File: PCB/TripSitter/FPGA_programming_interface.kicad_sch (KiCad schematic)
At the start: 10 parts, among them IC1 MT25QL256ABA1EW9-0SIT, J1 Conn_ARM_JTAG_SWD_20, U1 XC7A100T-FGG484

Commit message: before
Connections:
- net +3V3 is gone; now on net +3.3V: J1.2 (VCC/NC), R38.1, U1.U11 (M0_0)
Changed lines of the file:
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@@
   (junction (at 147.32 44.45) (diameter 0) (color 0 0 0 0)
   )
+  (junction (at 181.61 92.71) (diameter 0) (color 0 0 0 0)
+  )
   (junction (at 101.6 57.15) (diameter 0) (color 0 0 0 0)
   )
@@
   )
   (junction (at 184.15 142.24) (diameter 0) (color 0 0 0 0)
-  )
-  (junction (at 181.61 92.71) (diameter 0) (color 0 0 0 0)
   )
   (junction (at 43.18 95.25) (diameter 0) (color 0 0 0 0)
@@
     )
   )
-  (symbol (lib_id "fpga-rescue:+3.3V-power") (at 181.61 92.71 0) (unit 1)
-    (in_bom yes) (on_board yes) (dnp no)
-    (property "Reference" "#PWR047" (at 181.61 96.52 0)
-      (effects (font (size 1.27 1.27)) hide)
-    )
-    (property "Value" "+3.3V" (at 181.61 89.154 0)
-      (effects (font (size 1.27 1.27)))
-    )
-    (property "Footprint" "" (at 181.61 92.71 0)
-      (effects (font (size 1.27 1.27)) hide)
-    )
-    (property "Datasheet" "" (at 181.61 92.71 0)
-      (effects (font (size 1.27 1.27)) hide)
-    )
-    (pin "1")
-    (instances
-      (project "TripSitter"
-        (path "/5ab65702-9689-4dfd-8f10-6407062323a6/095fe883-dc50-4e06-a886-995eeb7c2300/a589e109-056b-42fc-a935-6e0e623ed03d"
-          (reference "#PWR047") (unit 1)
-        )
-      )
-      (project "fpga"
-        (path "/6f02ba16-07ff-46df-8179-c80a375dc867"
-          (reference "#PWR0302") (unit 1)
-        )
-      )
-    )
-  )
   (symbol (lib_id "Device:C_Small") (at 86.36 44.45 0) (unit 1)
     (in_bom yes) (on_board yes) (dnp no) (fields_autoplaced)
@@
         )
       )
+    )
+  )
+  (symbol (lib_id "power:+3.3V") (at 181.61 92.71 0) (mirror y) (unit 1)
+    (in_bom yes) (on_board yes) (dnp no)
+    (property "Reference" "#PWR011" (at 181.61 96.52 0)
+      (effects (font (size 1.27 1.27)) hide)
+    )
+    (property "Value" "+3.3V" (at 181.61 87.63 0)
+      (effects (font (size 1.27 1.27)))
+    )
+    (property "Footprint" "" (at 181.61 92.71 0)
+      (effects (font (size 1.27 1.27)) hide)
+    )
+    (property "Datasheet" "" (at 181.61 92.71 0)
+      (effects (font (size 1.27 1.27)) hide)
+    )
+    (pin "1")
+    (instances
+      (project "TripSitter"
+        (path "/5ab65702-9689-4dfd-8f10-6407062323a6/095fe883-dc50-4e06-a886-995eeb7c2300"
+          (reference "#PWR011") (unit 1)
+        )
+        (path "/5ab65702-9689-4dfd-8f10-6407062323a6/095fe883-dc50-4e06-a886-995eeb7c2300/ae3612c6-9651-4a37-8de7-7277774520fa"
+          (reference "#PWR014") (unit 1)
+        )
+        (path "/5ab65702-9689-4dfd-8f10-6407062323a6/095fe883-dc50-4e06-a886-995eeb7c2300/a589e109-056b-42fc-a935-6e0e623ed03d"
+          (reference "#PWR065") (unit 1)
+        )
+      )

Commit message: more pcb routing
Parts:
- added R20, R21: 10k, Resistor_SMD:R_0805_2012Metric_Pad1.20x1.40mm_HandSolder, symbol Device:R
- added R23, R24: 4.7k, Resistor_SMD:R_0603_1608Metric_Pad0.98x0.95mm_HandSolder, symbol Device:R
- C39: footprint Capacitor_SMD:C_1210_3225Metric_Pad1.33x2.70mm_HandSolder -> Capacitor_SMD:C_0603_1608Metric_Pad1.08x0.95mm_HandSolder; Component name CL21A476MQYNNNG -> CL10A476MR8NZNE; DK_Detail_Page https://www.digikey.no/product-detail/no/murata-electronics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 -> https://www.digikey.no/no/products/detail/samsung-electro-m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
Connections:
- net +3.3V: now also R20.1, R21.2
- net FPGA_PROGRAM_B: now also R24.1
- net at J1.7 (TMS/SWDIO), U1.T13 (TMS_0): now also R20.2
- net at U1.U12 (INIT_B_0): now also R23.1
- net at J1.9 (TCK/SWDCLK), U1.V12 (TCK_0): now also R21.1
- new net +3V3: R23.2, R24.2
- no-connect marks 15 -> 14

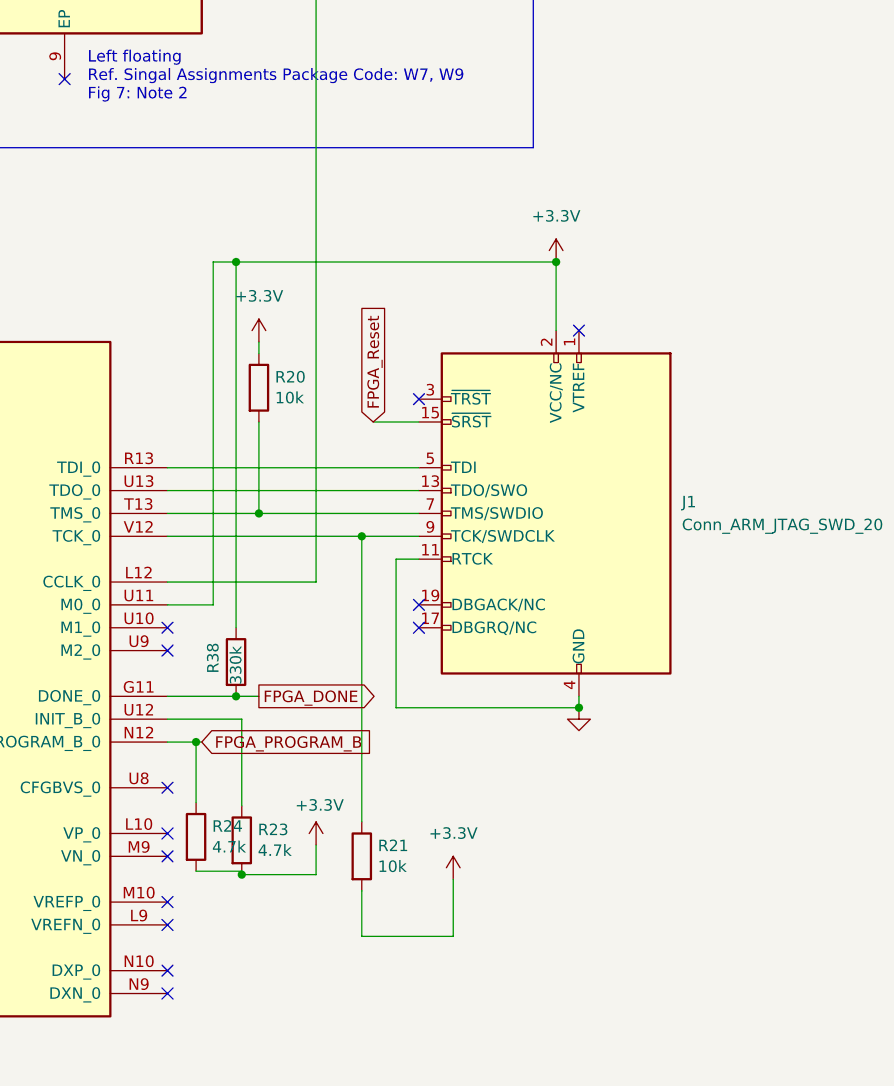
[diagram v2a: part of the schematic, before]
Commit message: pcb: Finalized routing without DDR3
Added ground and power plane, layed out all the components, fanned out
BGA. QSPI between FPGA->MCU->SRAM and MCU->SRAM is routed. Most is done
but DRC does not pass so do not produce.
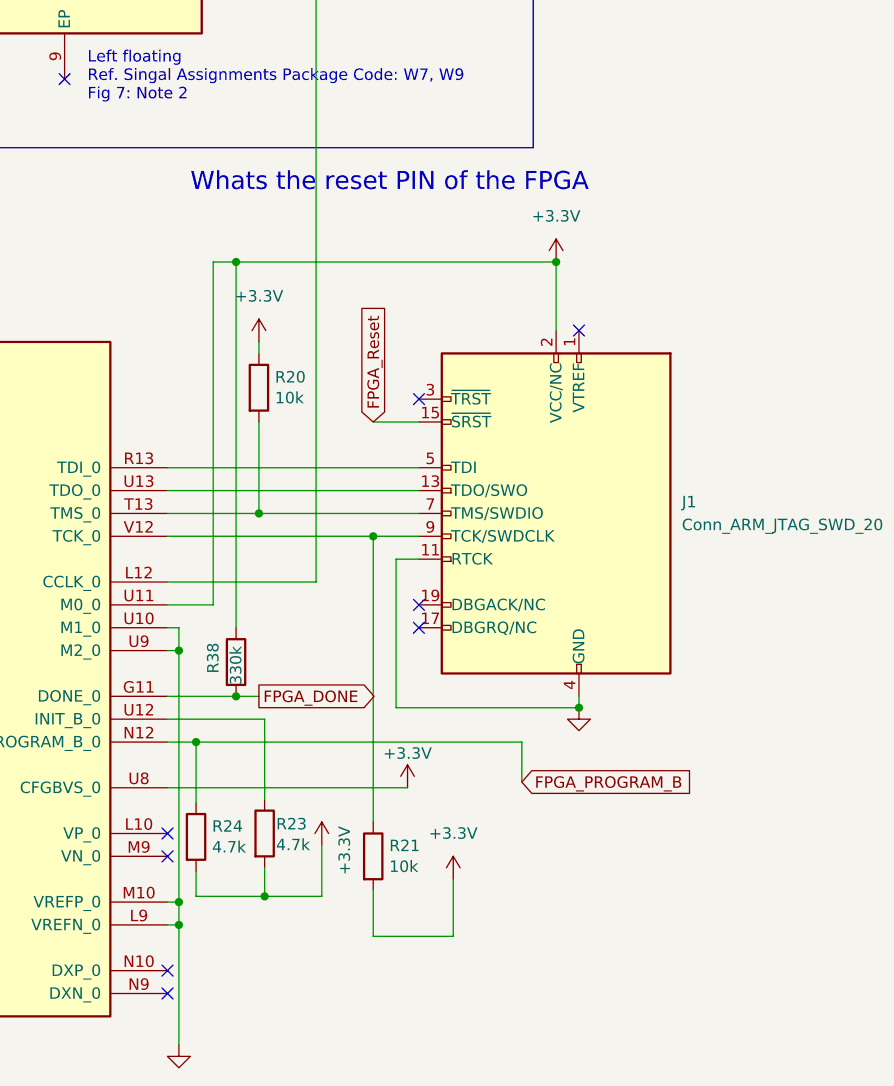
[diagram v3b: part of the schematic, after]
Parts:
- J1: footprint Connector_PinHeader_1.00mm:PinHeader_2x10_P1.00mm_Vertical -> Connector_PinHeader_2.54mm:PinHeader_2x07_P2.54mm_Vertical_SMD
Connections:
- net +3V3 is gone; now on net +3.3V: R23.2, R24.2
- net +3.3V: now also U1.U8 (CFGBVS_0)
- net GND: now also U1.L9 (VREFN_0), U1.M10 (VREFP_0), U1.U10 (M1_0), U1.U9 (M2_0)
- no-connect marks 14 -> 9
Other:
- note added: "Whats the reset PIN of the FPGA"
- moved on the sheet: R21, R23

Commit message: mcu debug edit
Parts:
- removed J1: Conn_ARM_JTAG_SWD_20, Connector_PinHeader_2.54mm:PinHeader_2x07_P2.54mm_Vertical_SMD, symbol Connector:Conn_ARM_JTAG_SWD_20
- added J4: Conn_02x07_Odd_Even, Connector_PinHeader_2.54mm:PinHeader_2x07_P2.54mm_Vertical_SMD, symbol Connector_Generic:Conn_02x07_Odd_Even
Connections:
- net +3.3V: now also J4.2 (Pin_2)
- net GND: now also J4.1 (Pin_1), J4.11 (Pin_11), J4.13 (Pin_13), J4.3 (Pin_3), J4.5 (Pin_5), J4.7 (Pin_7), J4.9 (Pin_9)
- net at R21.1, U1.V12 (TCK_0): now also J4.6 (Pin_6)
- net at U1.R13 (TDI_0): now also J4.10 (Pin_10)
- net at R20.2, U1.T13 (TMS_0): now also J4.4 (Pin_4)
- net at U1.U13 (TDO_0): now also J4.8 (Pin_8)
- no-connect marks 9 -> 7
